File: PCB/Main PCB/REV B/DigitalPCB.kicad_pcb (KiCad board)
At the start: 4 copper layers, 95 x 140 mm, 106 parts, among them J1 DF12NC-20DS-0.5V_51_, J2 1050170001, J3 Hopper, J4 Screen, J5 Spare1, J6 Spare2, Q1 MBT3904DW1, U1 AMS1117-3.3, U2 ESP32-WROOM-32UE_16MB, U3 TPS2115APWR, U4 TLP2362TPR_E, U5 CP2102N-A02-GQFN24, U6 TLP2362TPR_E, U7 TLP2362TPR_E, U8 STM811SW16F

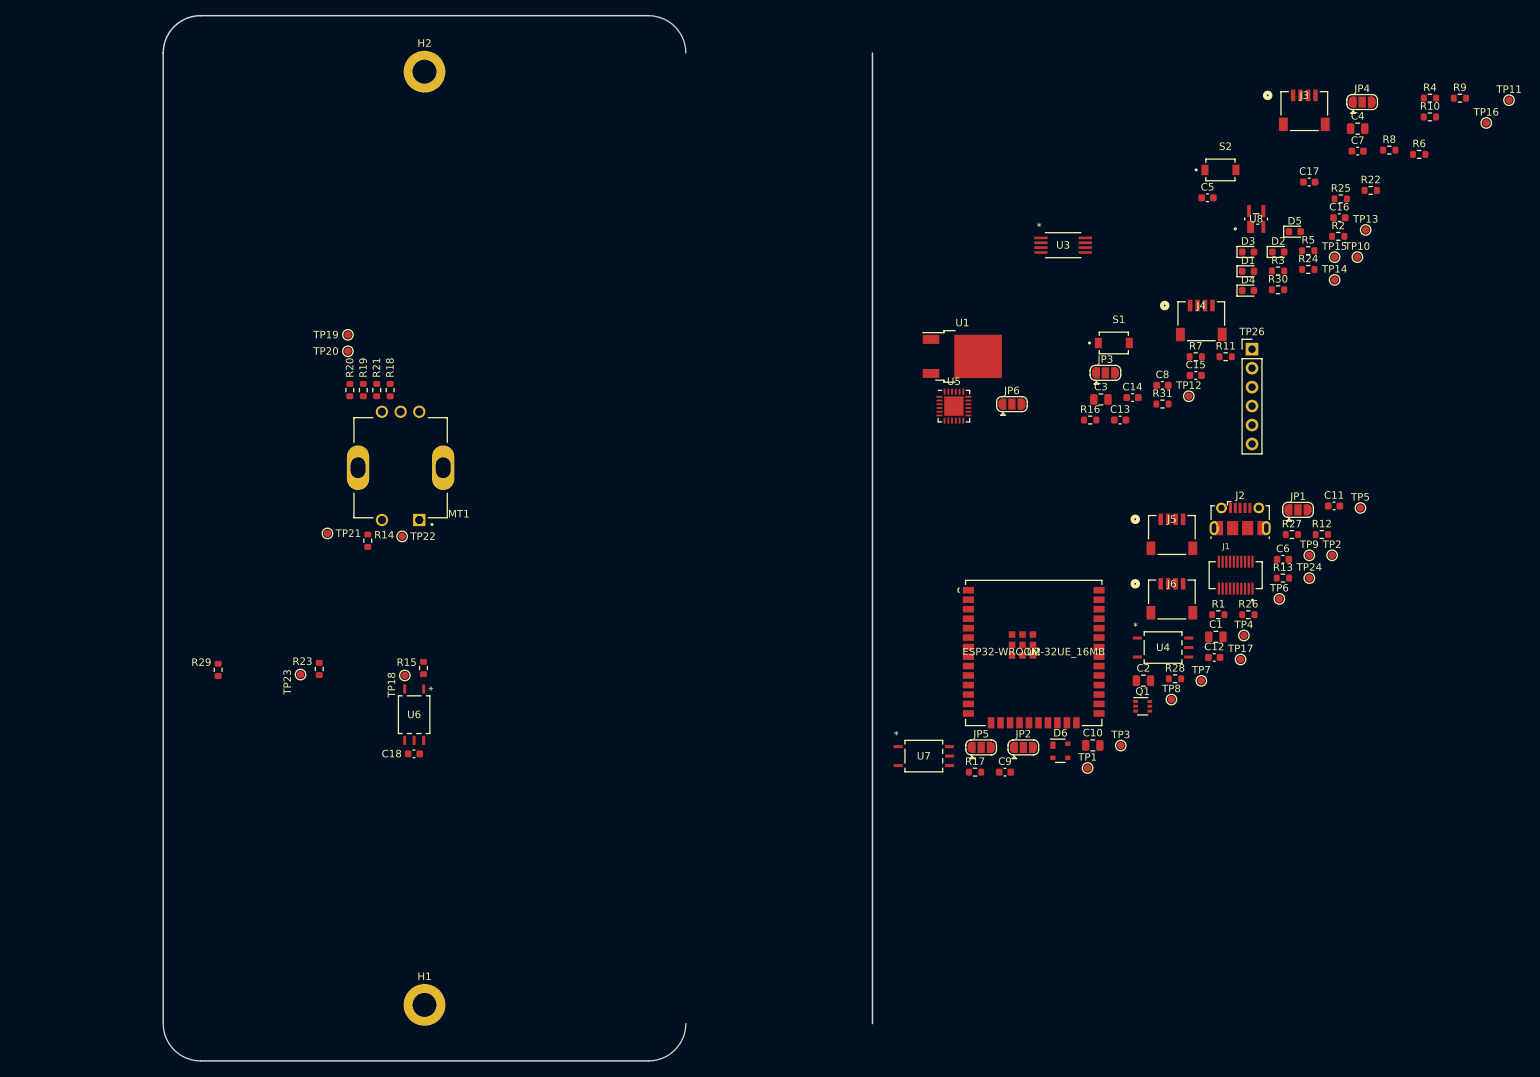
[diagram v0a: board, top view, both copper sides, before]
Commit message: PCB - Rough Analog Layout
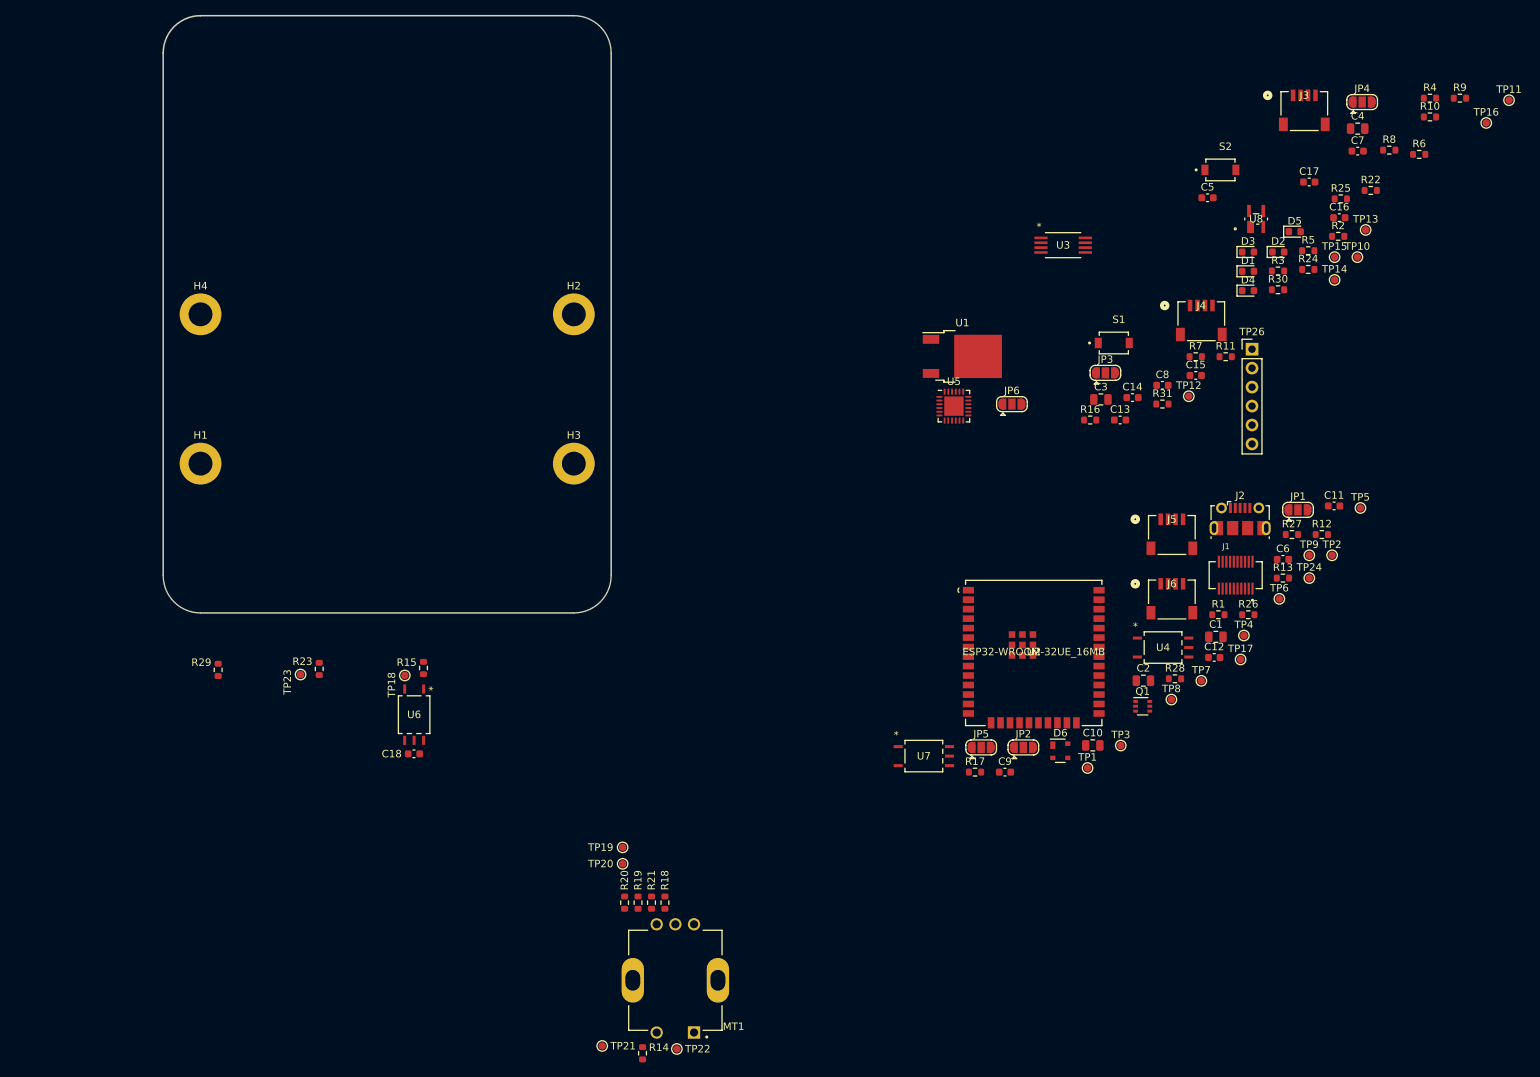
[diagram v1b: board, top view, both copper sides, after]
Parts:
- added H3: MountingHole, MountingHole:MountingHole_3.2mm_M3_DIN965_Pad, F.Cu at (105.0, 110.0)
- added H4: MountingHole, MountingHole:MountingHole_3.2mm_M3_DIN965_Pad, F.Cu at (55.0, 90.0)
- moved H1 78.5 mm to (55.0, 110.0)
- moved R21 77.9 mm to (115.4, 168.8)
- moved TP19 77.9 mm to (111.5, 161.4)
- moved R18 77.9 mm to (117.2, 168.8)
- moved R19 77.9 mm to (113.6, 168.8)
- moved R20 77.9 mm to (111.8, 168.8)
- moved TP20 77.9 mm to (111.5, 163.6)
- moved TP21 77.9 mm to (108.8, 188.0)
- moved TP22 77.9 mm to (118.8, 188.4)
- moved MT1 77.9 mm to (118.6, 179.2)
- moved R14 77.9 mm to (114.2, 189.0)
- moved H2 38.2 mm to (105.0, 90.0)
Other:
- board size 95 x 140 mm -> 60 x 80 mm
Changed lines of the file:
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@@
   )
   (footprint "TestPoint:TestPoint_Pad_D1.0mm" (layer "F.Cu")
-    (at 74.74 92.75)
+    (at 111.54 161.4)
     (descr "SMD pad as test Point, diameter 1.0mm")
     (tags "test point SMD pad")
@@
   )
   (footprint "MountingHole:MountingHole_3.2mm_M3_DIN965_Pad" locked (layer "F.Cu")
-    (at 85 182.5)
+    (at 55 110)
     (descr "Mounting Hole 3.2mm, M3, DIN965")
     (tags "mounting hole 3.2mm m3 din965")
@@
   )
   (footprint "Resistor_SMD:R_0603_1608Metric" (layer "F.Cu")
-    (at 75 100.15 -90)
+    (at 111.8 168.8 -90)
     (descr "Resistor SMD 0603 (1608 Metric), square (rectangular) end terminal, IPC_7351 nominal, (Body size source: IPC-SM-782 page 72, https://www.pcb-3d.com/wordpress/wp-content/uploads/ipc-sm-782a_amendment_1_and_2.pdf), generated with kicad-footprint-generator")
     (tags "resistor")
@@
   )
   (footprint "TestPoint:TestPoint_Pad_D1.0mm" (layer "F.Cu")
-    (at 74.74 94.95)
+    (at 111.54 163.6)
     (descr "SMD pad as test Point, diameter 1.0mm")
     (tags "test point SMD pad")
@@
   )
   (footprint "Customs Smoker:XDCR_PEC11R-4215F-S0024" (layer "F.Cu")
-    (at 81.8 110.55 180)
+    (at 118.6 179.2 180)
     (property "Manufacturer" "Bourns Inc.")
     (property "Manufacturer Part Number" "PEC11R-4220K-S0024")
@@
   )
   (footprint "MountingHole:MountingHole_3.2mm_M3_DIN965_Pad" locked (layer "F.Cu")
-    (at 85 57.5)
+    (at 105 90)
     (descr "Mounting Hole 3.2mm, M3, DIN965")
     (tags "mounting hole 3.2mm m3 din965")
@@
   )
   (footprint "Resistor_SMD:R_0603_1608Metric" (layer "F.Cu")
-    (at 80.4 100.15 90)
+    (at 117.2 168.8 90)
     (descr "Resistor SMD 0603 (1608 Metric), square (rectangular) end terminal, IPC_7351 nominal, (Body size source: IPC-SM-782 page 72, https://www.pcb-3d.com/wordpress/wp-content/uploads/ipc-sm-782a_amendment_1_and_2.pdf), generated with kicad-footprint-generator")
     (tags "resistor")
@@
   )
   (footprint "Resistor_SMD:R_0603_1608Metric" (layer "F.Cu")
-    (at 77.4 120.325 -90)
+    (at 114.2 188.975 -90)
     (descr "Resistor SMD 0603 (1608 Metric), square (rectangular) end terminal, IPC_7351 nominal, (Body size source: IPC-SM-782 page 72, https://www.pcb-3d.com/wordpress/wp-content/uploads/ipc-sm-782a_amendment_1_and_2.pdf), generated with kicad-footprint-generator")
     (tags "resistor")
@@
   )
   (footprint "Resistor_SMD:R_0603_1608Metric" (layer "F.Cu")
-    (at 76.8 100.15 90)
+    (at 113.6 168.8 90)
     (descr "Resistor SMD 0603 (1608 Metric), square (rectangular) end terminal, IPC_7351 nominal, (Body size source: IPC-SM-782 page 72, https://www.pcb-3d.com/wordpress/wp-content/uploads/ipc-sm-782a_amendment_1_and_2.pdf), generated with kicad-footprint-generator")
     (tags "resistor")
@@
   )
   (footprint "Resistor_SMD:R_0603_1608Metric" (layer "F.Cu")
-    (at 78.6 100.15 -90)
+    (at 115.4 168.8 -90)
     (descr "Resistor SMD 0603 (1608 Metric), square (rectangular) end terminal, IPC_7351 nominal, (Body size source: IPC-SM-782 page 72, https://www.pcb-3d.com/wordpress/wp-content/uploads/ipc-sm-782a_amendment_1_and_2.pdf), generated with kicad-footprint-generator")
     (tags "resistor")
@@
     )
   )
+  (footprint "MountingHole:MountingHole_3.2mm_M3_DIN965_Pad" (layer "F.Cu")
+    (at 105 110)
+    (descr "Mounting Hole 3.2mm, M3, DIN965")
+    (tags "mounting hole 3.2mm m3 din965")
+    (property "Sheetfile" "DigitalPCB.kicad_sch")
+    (property "Sheetname" "")
+    (attr exclude_from_pos_files)
+    (fp_text reference "H3" (at 0 -3.8) (layer "F.SilkS")
+      (effects (font (size 1 1) (thickness 0.15)))
+    )
+    (fp_text value "MountingHole" (at 0 3.8) (layer "F.Fab")
+      (effects (font (size 1 1) (thickness 0.15)))
+    )
+    (fp_text user "${REFERENCE}" (at 0 0) (layer "F.Fab")
+      (effects (font (size 1 1) (thickness 0.15)))
+    )
+    (fp_circle (center 0 0) (end 2.8 0) (layer "Cmts.User") (width 0.15) (fill none))
+    (fp_circle (center 0 0) (end 3.05 0) (layer "F.CrtYd") (width 0.05) (fill none))
+    (pad "1" thru_hole circle (at 0 0) (size 5.6 5.6) (drill 3.2) (layers *.Cu *.Mask))
+  )
   (footprint "Resistor_SMD:R_0603_1608Metric" (layer "F.Cu")
     (at 218.23 68.58)
@@
   )
   (footprint "TestPoint:TestPoint_Pad_D1.0mm" (layer "F.Cu")
-    (at 82 119.75)
+    (at 118.8 188.4)
     (descr "SMD pad as test Point, diameter 1.0mm")
     (tags "test point SMD pad")
@@
   )
   (footprint "TestPoint:TestPoint_Pad_D1.0mm" (layer "F.Cu")
-    (at 72 119.35)
+    (at 108.8 188)
     (descr "SMD pad as test Point, diameter 1.0mm")
     (tags "test point SMD pad")
@@
     )
   )
+  (footprint "MountingHole:MountingHole_3.2mm_M3_DIN965_Pad" (layer "F.Cu")
+    (at 55 90)
+    (descr "Mounting Hole 3.2mm, M3, DIN965")
+    (tags "mounting hole 3.2mm m3 din965")
+    (property "Sheetfile" "DigitalPCB.kicad_sch")
+    (property "Sheetname" "")
+    (attr exclude_from_pos_files)
+    (fp_text reference "H4" (at 0 -3.8) (layer "F.SilkS")
+      (effects (font (size 1 1) (thickness 0.15)))
+    )
+    (fp_text value "MountingHole" (at 0 3.8) (layer "F.Fab")
+      (effects (font (size 1 1) (thickness 0.15)))
+    )
+    (fp_text user "${REFERENCE}" (at 0 0) (layer "F.Fab")
+      (effects (font (size 1 1) (thickness 0.15)))
+    )
+    (fp_circle (center 0 0) (end 2.8 0) (layer "Cmts.User") (width 0.15) (fill none))
+    (fp_circle (center 0 0) (end 3.05 0) (layer "F.CrtYd") (width 0.05) (fill none))
+    (pad "1" thru_hole circle (at 0 0) (size 5.6 5.6) (drill 3.2) (layers *.Cu *.Mask))
+  )
   (footprint "TestPoint:TestPoint_Pad_D1.0mm" (layer "F.Cu")
     (at 194.75 133.02)
@@
       ))
   )
-  (gr_arc locked (start 115 50) (mid 118.535534 51.464466) (end 120 55) (layer "Edge.Cuts") (width 0.1))
-  (gr_line locked (start 115 50) (end 55 50) (layer "Edge.Cuts") (width 0.2))
+  (gr_arc locked (start 105 50) (mid 108.535534 51.464466) (end 110 55) (layer "Edge.Cuts") (width 0.1))
+  (gr_line locked (start 105 50) (end 55 50) (layer "Edge.Cuts") (width 0.2))
   (gr_arc locked (start 50 55) (mid 51.464466 51.464466) (end 55 50) (layer "Edge.Cuts") (width 0.2))
-  (gr_arc locked (start 55 190) (mid 51.464466 188.535534) (end 50 185) (layer "Edge.Cuts") (width 0.1))
-  (gr_line locked (start 55 190) (end 115 190) (layer "Edge.Cuts") (width 0.2))
-  (gr_line locked (start 145 185) (end 145 55) (layer "Edge.Cuts") (width 0.2))
-  (gr_arc locked (start 120 185) (mid 118.535534 188.535534) (end 115 190) (layer "Edge.Cuts") (width 0.1))
-  (gr_line locked (start 50 55) (end 50 185) (layer "Edge.Cuts") (width 0.2))
+  (gr_arc locked (start 55 130) (mid 51.464466 128.535534) (end 50 125) (layer "Edge.Cuts") (width 0.1))
+  (gr_line locked (start 55 130) (end 105 130) (layer "Edge.Cuts") (width 0.2))
+  (gr_line locked (start 110 125) (end 110 55) (layer "Edge.Cuts") (width 0.2))
+  (gr_arc locked (start 110 125) (mid 108.535534 128.535534) (end 105 130) (layer "Edge.Cuts") (width 0.1))
+  (gr_line locked (start 50 55) (end 50 125) (layer "Edge.Cuts") (width 0.2))
   (group "" (id 6990c1ee-598c-46b5-9838-bfa1b053bca3)
     (members

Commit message: PCB - Digital layout nearly complete
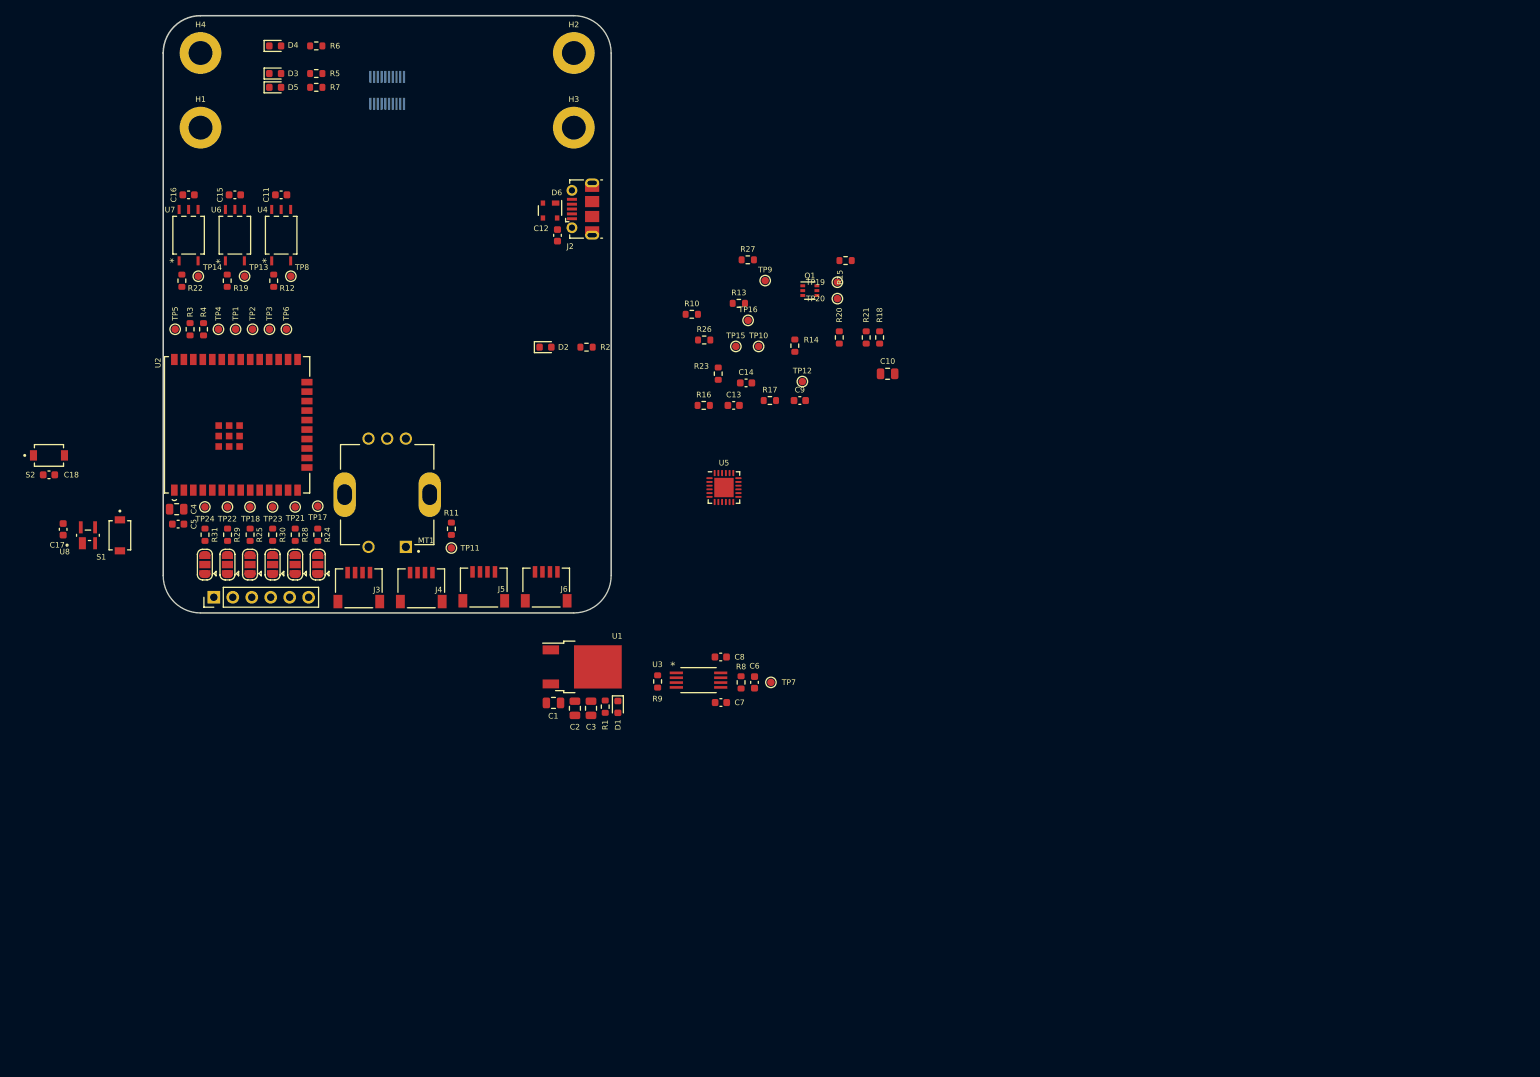
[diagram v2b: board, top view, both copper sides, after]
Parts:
- J1: moved to B.Cu
- moved C17 173.3 mm to (36.6, 118.8), turned to 90 degrees
- moved R4 167.2 mm to (55.4, 92.0), turned to 90 degrees
- moved C4 166.2 mm to (51.8, 116.1)
- moved JP4 164.1 mm to (58.6, 123.5), turned to 90 degrees
- moved U8 162.1 mm to (39.9, 119.6)
- moved S2 161.5 mm to (34.7, 108.9)
- moved TP5 160.6 mm to (51.6, 92.0), turned to 90 degrees
- moved R22 159.7 mm to (52.5, 85.5), turned to 90 degrees
- moved C16 154.2 mm to (53.4, 74.0)
- moved TP11 153.8 mm to (88.6, 121.3)
- moved R25 152.9 mm to (61.6, 119.5), turned to -90 degrees
- moved TP14 152.2 mm to (54.7, 84.9), turned to 90 degrees
- moved TP13 150.3 mm to (60.9, 84.9), turned to 90 degrees
- moved R6 148.4 mm to (70.5, 54.0), turned to 180 degrees
- moved TP24 148.2 mm to (55.6, 115.8)
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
